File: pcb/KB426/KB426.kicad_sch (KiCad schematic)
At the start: 159 parts, among them J1 Conn_01x03_Socket, SW1 SW_Push_45deg, SW10 SW_Push_45deg, SW11 SW_Push_45deg, SW12 SW_Push_45deg, SW13 SW_Push_45deg, SW14 SW_Push_45deg, SW15 SW_Push_45deg, SW16 SW_Push_45deg, SW17 SW_Push_45deg, SW18 SW_Push_45deg, SW19 SW_Push_45deg, SW2 SW_Push_45deg, SW20 SW_Push_45deg, SW21 SW_Push_45deg, SW22 SW_Push_45deg, SW23 SW_Push_45deg, SW24 SW_Push_45deg, SW25 SW_Push_45deg, SW26 SW_Push_45deg, SW27 SW_Push_45deg, SW28 SW_Push_45deg, SW29 SW_Push_45deg, SW3 SW_Push_45deg, SW30 SW_Push_45deg, SW31 SW_Push_45deg, SW32 SW_Push_45deg, SW33 SW_Push_45deg, SW34 SW_Push_45deg, SW35 SW_Push_45deg, SW36 SW_Push_45deg, SW37 SW_Push_45deg, SW38 SW_Push_45deg, SW39 SW_Push_45deg, SW4 SW_Push_45deg, SW40 SW_Push_45deg, SW41 SW_Push_45deg, SW42 SW_Push_45deg, SW43 SW_Push_45deg, SW44 SW_Push_45deg, SW45 SW_Push_45deg, SW46 SW_Push_45deg, SW47 RotaryEncoder_Switch, SW48 SW_Push_45deg, SW49 SW_Push_45deg, SW5 SW_Push_45deg, SW50 SW_Push_45deg, SW51 SW_Push_45deg, SW52 SW_Push_45deg, SW53 SW_Push_45deg, SW54 SW_Push_45deg, SW55 SW_Push_45deg, SW56 SW_Push_45deg, SW57 SW_Push_45deg, SW58 SW_Push_45deg, SW59 SW_Push_45deg, SW6 SW_Push_45deg, SW60 SW_Push_45deg, SW61 SW_Push_45deg, SW62 SW_Push_45deg, SW63 SW_Push_45deg, SW64 SW_Push_45deg, SW65 SW_Push_45deg, SW66 SW_Push_45deg, SW67 SW_Push_45deg, SW68 SW_Push_45deg, SW7 SW_Push_45deg, SW8 SW_Push_45deg, SW9 SW_Push_45deg, U1 Pico

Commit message: update pcb
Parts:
- removed D64: 1N4148, Diode_THT:D_DO-35_SOD27_P7.62mm_Horizontal, symbol Diode:1N4148
- removed H11: MountingHole, MountingHole:MountingHole_2.2mm_M2_Pad, symbol Mechanical:MountingHole
- removed J1: Conn_01x03_Socket, Connector_PinHeader_2.54mm:PinHeader_1x03_P2.54mm_Vertical, symbol Connector:Conn_01x03_Socket
- removed ST7735S_80x160_SPI1: ~, SPI_Displays:ST7735S_80x160_SPI, symbol SPI_Displays:ST7735S_80x160_SPI
- removed SW64: SW_Push_45deg, PCM_Switch_Keyboard_Cherry_MX:SW_Cherry_MX_PCB_1.00u, symbol Switch:SW_Push_45deg
- added D47, D48: 1N4148, Diode_THT:D_DO-35_SOD27_P7.62mm_Horizontal, symbol Diode:1N4148
- added D70: LED, LED_THT:LED_D5.0mm, symbol Device:LED
- added J3: Conn_01x06_Socket, Connector_PinHeader_2.54mm:PinHeader_2x03_P2.54mm_Vertical, symbol Connector:Conn_01x06_Socket
- added R5: 390, Resistor_THT:R_Axial_DIN0207_L6.3mm_D2.5mm_P10.16mm_Horizontal, symbol Device:R
- added SSD1306_128x32_i2c1: ~, SPI_Displays:SSD1306_128x32_i2c, symbol SPI_Displays:ssd1306_128x32_i2c
- added SW47, SW69: SW_Push_45deg, PCM_Switch_Keyboard_Cherry_MX:SW_Cherry_MX_PCB_1.00u, symbol Switch:SW_Push_45deg
- C1, C2: footprint Capacitor_SMD:C_1206_3216Metric_Pad1.33x1.80mm_HandSolder -> Capacitor_THT:C_Disc_D3.0mm_W1.6mm_P2.50mm
- SW60: footprint PCM_Switch_Keyboard_Cherry_MX:SW_Cherry_MX_PCB_1.00u -> PCM_Switch_Keyboard_Cherry_MX:SW_Cherry_MX_PCB_2.25u
- SW61: footprint PCM_Switch_Keyboard_Cherry_MX:SW_Cherry_MX_PCB_2.25u -> PCM_Switch_Keyboard_Cherry_MX:SW_Cherry_MX_PCB_1.00u
- SW66: footprint PCM_Switch_Keyboard_Cherry_MX:SW_Cherry_MX_PCB_1.00u -> PCM_Switch_Keyboard_Cherry_MX:SW_Cherry_MX_PCB_1.75u
- SW68: footprint PCM_Switch_Keyboard_Cherry_MX:SW_Cherry_MX_PCB_1.75u -> PCM_Switch_Keyboard_Cherry_MX:SW_Cherry_MX_PCB_1.00u
- renumbered D48 to D64, D47 to D69, D100 to D71, R5 to R6, SW47 to SW48, SW48 to SW64
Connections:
- net +3V3: now also R5.1, SSD1306_128x32_i2c1.2 (VCC)
- net Col 1: now also SW56.2, SW63.2, J3.6 (Pin_6); no longer SW57.2, SW65.2
- net Col 2: now also SW57.2, SW64.2, J3.2 (Pin_2); no longer SW58.2, SW66.2
- net Col 3: now also SW58.2, SW65.2; no longer SW59.2, SW67.2
- net Col 4: now also SW59.2, SW66.2; no longer SW60.2, SW68.2
- net Col 5: now also SW60.2, SW67.2; no longer SW61.2
- net Col 6: now also SW61.2, SW68.2; no longer SW62.2
- net Col 7: now also SW62.2, SW47.2, SW69.2; no longer SW48.S2, SW63.2
- net Col 8: now also SW48.S1; no longer SW56.2, SW64.2
- net GND: now also D70.1 (K), J3.3 (Pin_3), J3.4 (Pin_4), SSD1306_128x32_i2c1.1 (GND)
- net Row 6: now also D47.1 (K), D48.1 (K); no longer D69.1 (K)
- net Row 7: no longer D56.1 (K)
- net Row 8: now also D56.1 (K); no longer D63.1 (K), D64.1 (K)
- net Row 9: now also D63.1 (K), D64.1 (K), D69.1 (K)
- net at U1.24 (GPIO18): now also SSD1306_128x32_i2c1.3 (SCK)
- net at U1.25 (GPIO19): now also SSD1306_128x32_i2c1.4 (SDA)
- net at U1.41 (SWCLK): now also J3.1 (Pin_1)
- net at U1.43 (SWDIO): now also J3.5 (Pin_5)
- net at D69.2 (A): now also SW69.1; no longer SW48.S1
- new net: D47.2 (A), SW47.1
- new net: D70.2 (A), R5.2
- new net: D48.2 (A), SW48.S2
- no-connect marks 1 -> 0
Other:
- moved on the sheet: C1, C2, D55, D56, D57, D58, D59, D60, D61, D62, D63, D64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

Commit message: + update pcb
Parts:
- added J2: Conn_01x03_Socket, Connector_PinHeader_2.54mm:PinHeader_1x03_P2.54mm_Vertical, symbol Connector:Conn_01x03_Socket
- renumbered C2 to C1, C1 to C2, J3 to J1, R4 to R1, R3 to R2, R2 to R3, R1 to R4
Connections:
- net +5V: now also U1.39 (VSYS), J2.1 (Pin_1)
- net Col 1: no longer J1.6 (Pin_6)
- net Col 2: no longer J1.2 (Pin_2)
- net GND: now also J2.3 (Pin_3)
- net Rot CLK: now also U1.31 (GPIO26_ADC0); no longer U1.32 (GPIO27_ADC1)
- net Rot DT: now also U1.29 (GPIO22); no longer U1.34 (GPIO28_ADC2)
- net Row 9: now also U1.24 (GPIO18); no longer U1.21 (GPIO16)
- net at U1.22 (GPIO17): now also J1.2 (Pin_2)
- net at SSD1306_128x32_i2c1.3 (SCK): now also U1.27 (GPIO21); no longer U1.24 (GPIO18)
- net at U1.25 (GPIO19): now also J2.2 (Pin_2); no longer SSD1306_128x32_i2c1.4 (SDA)
- net at U1.26 (GPIO20): now also SSD1306_128x32_i2c1.4 (SDA)
- net at R6.1: now also U1.32 (GPIO27_ADC1); no longer U1.29 (GPIO22)
- net at U1.41 (SWCLK): now also J1.5 (Pin_5); no longer J1.1 (Pin_1)
- net at U1.43 (SWDIO): now also J1.1 (Pin_1); no longer J1.5 (Pin_5)
- new net: J1.6 (Pin_6), U1.21 (GPIO16)
- no-connect marks 0 -> 4
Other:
- moved on the sheet: D71, H1, H10, H2, H3, H4, H5, H6, H7, H8, H9, J1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

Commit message: pcb v1
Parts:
- removed J2: Conn_01x03_Socket, Connector_PinHeader_2.54mm:PinHeader_1x03_P2.54mm_Vertical, symbol Connector:Conn_01x03_Socket
- added C10, C11, C12, C13, C14, C15, C16, C17, C18, C3, C4, C5, C6, C7, C8, C9: 100nF, Capacitor_SMD:C_0603_1608Metric, symbol Device:C_45deg
- added D72, D73, D74, D75, D76, D77, D78, D79, D80, D81, D82, D83, D84, D85, D86, D87: WS2812B, LED_SMD:LED_WS2812B_PLCC4_5.0x5.0mm_P3.2mm, symbol LED:WS2812B
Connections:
- net +5V: now also C10.2, C11.2, C12.2, C13.2, C14.2, C15.2, C16.2, C17.2, C18.2, C3.2, C4.2, C5.2, C6.2, C7.2, C8.2, C9.2, D72.1 (VDD), D73.1 (VDD), D74.1 (VDD), D75.1 (VDD), D76.1 (VDD), D77.1 (VDD), D78.1 (VDD), D79.1 (VDD), D80.1 (VDD), D81.1 (VDD), D82.1 (VDD), D83.1 (VDD), D84.1 (VDD), D85.1 (VDD), D86.1 (VDD), D87.1 (VDD)
- net GND: now also C10.1, C11.1, C12.1, C13.1, C14.1, C15.1, C16.1, C17.1, C18.1, C3.1, C4.1, C5.1, C6.1, C7.1, C8.1, C9.1, D72.3 (VSS), D73.3 (VSS), D74.3 (VSS), D75.3 (VSS), D76.3 (VSS), D77.3 (VSS), D78.3 (VSS), D79.3 (VSS), D80.3 (VSS), D81.3 (VSS), D82.3 (VSS), D83.3 (VSS), D84.3 (VSS), D85.3 (VSS), D86.3 (VSS), D87.3 (VSS)
- net uart rx: now reaches J1.6 (Pin_6)
- net uart rx: now also U1.22 (GPIO17); no longer U1.21 (GPIO16)
- net uart tx: now reaches J1.2 (Pin_2)
- net uart tx: now also U1.21 (GPIO16); no longer U1.22 (GPIO17)
- net leds: now reaches U1.25 (GPIO19)
- net leds: now also D72.4 (DIN)
- net swclk: now reaches J1.5 (Pin_5), U1.41 (SWCLK)
- net swdio: now reaches J1.1 (Pin_1), U1.43 (SWDIO)
- new net: D75.2 (DOUT), D76.4 (DIN)
- new net: D74.2 (DOUT), D75.4 (DIN)
- new net: D73.2 (DOUT), D74.4 (DIN)
- new net: D72.2 (DOUT), D73.4 (DIN)
- new net: D86.2 (DOUT), D87.4 (DIN)
- new net: D76.2 (DOUT), D77.4 (DIN)
- new net: D77.2 (DOUT), D78.4 (DIN)
- new net: D81.2 (DOUT), D82.4 (DIN)
- new net: D80.2 (DOUT), D81.4 (DIN)
- new net: D83.2 (DOUT), D84.4 (DIN)
- new net: D82.2 (DOUT), D83.4 (DIN)
- new net: D79.2 (DOUT), D80.4 (DIN)
- new net: D78.2 (DOUT), D79.4 (DIN)
- new net: D85.2 (DOUT), D86.4 (DIN)
- new net: D84.2 (DOUT), D85.4 (DIN)
- no-connect marks 4 -> 5
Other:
- moved on the sheet: D71, R6, SSD1306_128x32_i2c1

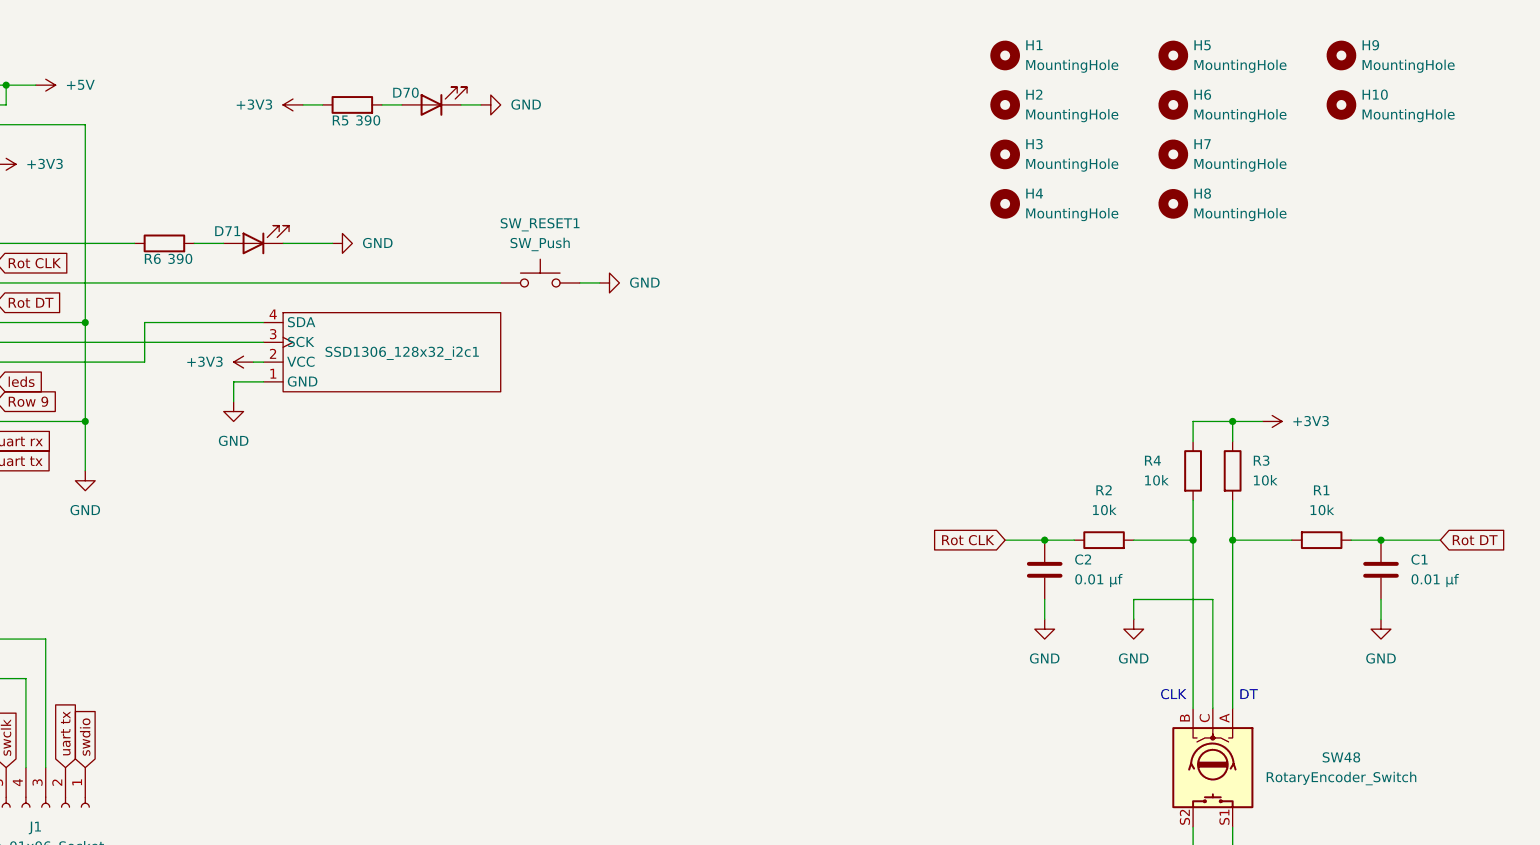
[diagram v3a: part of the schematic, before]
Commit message: fix ground plane, update serigraphie
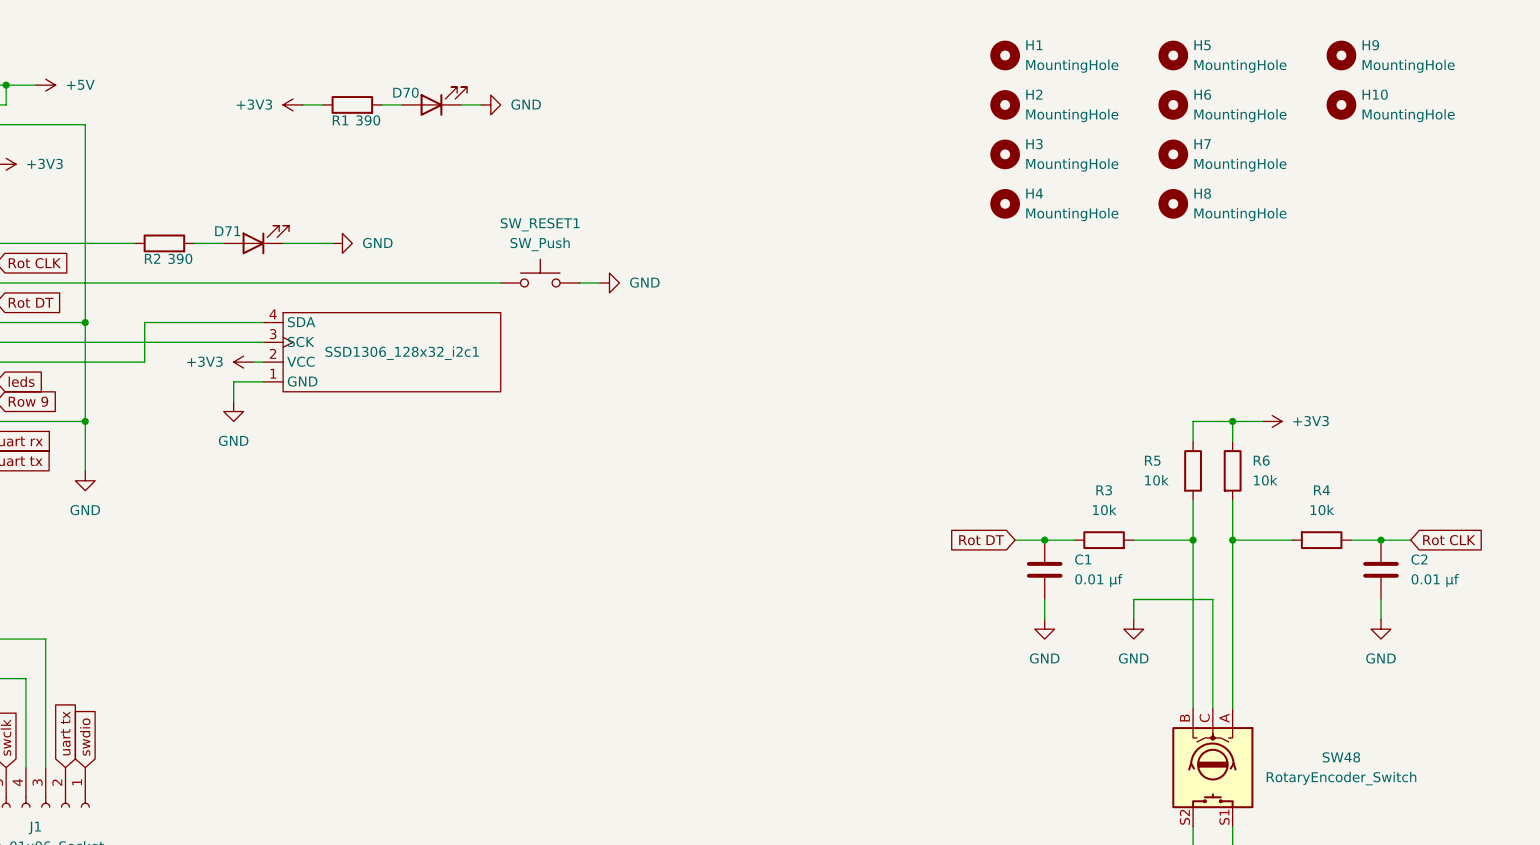
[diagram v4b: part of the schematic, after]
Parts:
- renumbered C2 to C1, C1 to C2, R5 to R1, R6 to R2, R2 to R3, R1 to R4, R4 to R5, R3 to R6
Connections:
- net Rot CLK: now also C2.1, R4.1; no longer C1.1, R3.1
- net Rot DT: now also C1.1, R3.1; no longer C2.1, R4.1
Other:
- note removed: "CLK"
- note removed: "DT"
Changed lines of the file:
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@@
 	)
 	(junction
+		(at 476.25 95.25)
+		(diameter 0)
+		(color 0 0 0 0)
+	)
+	(junction
 		(at 444.5 166.37)
 		(diameter 0)
@@
 	)
 	(junction
-		(at 519.43 95.25)
-		(diameter 0)
-		(color 0 0 0 0)
-	)
-	(junction
 		(at 317.5 219.71)
 		(diameter 0)
@@
 	)
 	(junction
+		(at 519.43 95.25)
+		(diameter 0)
+		(color 0 0 0 0)
+	)
+	(junction
 		(at 177.8 153.67)
 		(diameter 0)
@@
 	)
 	(junction
-		(at 476.25 95.25)
-		(diameter 0)
-		(color 0 0 0 0)
-	)
-	(junction
 		(at 203.2 207.01)
 		(diameter 0)
@@
 	(wire
 		(pts
-			(xy 471.17 95.25) (xy 476.25 95.25)
-		)
-		(stroke
-			(width 0)
-			(type default)
-		)
-	)
-	(wire
-		(pts
 			(xy 279.4 303.53) (xy 304.8 303.53)
 		)
@@
 	(wire
 		(pts
-			(xy 476.25 95.25) (xy 480.06 95.25)
+			(xy 472.44 95.25) (xy 476.25 95.25)
 		)
 		(stroke
@@
 	(wire
 		(pts
+			(xy 519.43 95.25) (xy 515.62 95.25)
+		)
+		(stroke
+			(width 0)
+			(type default)
+		)
+	)
+	(wire
+		(pts
 			(xy 508 248.92) (xy 203.2 248.92)
 		)
@@
 	(wire
 		(pts
+			(xy 476.25 95.25) (xy 480.06 95.25)
+		)
+		(stroke
+			(width 0)
+			(type default)
+		)
+	)
+	(wire
+		(pts
 			(xy 474.98 207.01) (xy 477.52 207.01)
 		)
@@
 	(wire
 		(pts
-			(xy 519.43 95.25) (xy 515.62 95.25)
+			(xy 523.24 95.25) (xy 519.43 95.25)
 		)
 		(stroke
@@
 	(wire
 		(pts
-			(xy 527.05 95.25) (xy 519.43 95.25)
-		)
-		(stroke
-			(width 0)
-			(type default)
-		)
-	)
-	(wire
-		(pts
 			(xy 375.92 67.31) (xy 360.68 67.31)
 		)
@@
 		)
 	)
-	(text "CLK\n"
-		(exclude_from_sim no)
-		(at 492.76 115.316 0)
-		(effects
-			(font
-				(size 1.27 1.27)
-			)
-		)
-	)
-	(text "DT"
-		(exclude_from_sim no)
-		(at 502.412 115.316 0)
-		(effects
-			(font
-				(size 1.27 1.27)
-			)
-		)
-	)
 	(global_label "swclk"
 		(shape input)
@@
 	(global_label "Rot DT"
 		(shape input)
-		(at 527.05 95.25 0)
+		(at 472.44 95.25 180)
 		(fields_autoplaced yes)
 		(effects
@@
 				(size 1.27 1.27)
 			)
-			(justify left)
+			(justify right)
 		)
 		(property "Intersheetrefs" "${INTERSHEET_REFS}"
-			(at 536.3851 95.25 0)
+			(at 463.1049 95.25 0)
 			(effects
 				(font
 					(size 1.27 1.27)
 				)
-				(justify left)
+				(justify right)
 				(hide yes)
 			)
@@
 	(global_label "Rot CLK"
 		(shape input)
-		(at 471.17 95.25 180)
+		(at 523.24 95.25 0)
 		(fields_autoplaced yes)
 		(effects
@@
 				(size 1.27 1.27)
 			)
-			(justify right)
+			(justify left)
 		)
 		(property "Intersheetrefs" "${INTERSHEET_REFS}"
-			(at 460.5044 95.25 0)
+			(at 533.9056 95.25 0)
 			(effects
 				(font
 					(size 1.27 1.27)
 				)
-				(justify right)
+				(justify left)
 				(hide yes)
 			)
@@
 		(dnp no)
 		(fields_autoplaced yes)
-		(property "Reference" "R3"
+		(property "Reference" "R6"
 			(at 502.92 85.0899 0)
 			(effects
@@
 			(project "KB426"
 				(path "/9a9ef932-5886-4734-ab54-818112b62564"
-					(reference "R3")
+					(reference "R6")
 					(unit 1)
 				)
@@
 		(on_board yes)
 		(dnp no)
-		(property "Reference" "R5"
+		(property "Reference" "R1"
 			(at 385.826 41.402 90)
 			(effects
@@
 			(project "KB426"
 				(path "/9a9ef932-5886-4734-ab54-818112b62564"
-					(reference "R5")
+					(reference "R1")
 					(unit 1)
 				)
@@
 		(dnp no)
 		(fields_autoplaced yes)
-		(property "Reference" "C1"
+		(property "Reference" "C2"
 			(at 523.24 97.7899 0)
 			(effects
@@
 			(project ""
 				(path "/9a9ef932-5886-4734-ab54-818112b62564"
-					(reference "C1")
+					(reference "C2")
 					(unit 1)
 				)
@@
 		(on_board yes)
 		(dnp no)
-		(property "Reference" "R6"
+		(property "Reference" "R2"
 			(at 361.696 59.182 90)
 			(effects
@@
 			(project "KB426"
 				(path "/9a9ef932-5886-4734-ab54-818112b62564"
-					(reference "R6")
+					(reference "R2")
 					(unit 1)
 				)
@@
 		(dnp no)
 		(fields_autoplaced yes)
-		(property "Reference" "R2"
+		(property "Reference" "R3"
 			(at 483.87 88.9 90)
 			(effects
@@
 			(project "KB426"
 				(path "/9a9ef932-5886-4734-ab54-818112b62564"
-					(reference "R2")
+					(reference "R3")
 					(unit 1)
 				)
@@
 		(dnp no)
 		(fields_autoplaced yes)
-		(property "Reference" "C2"
+		(property "Reference" "C1"
 			(at 480.06 97.7899 0)
 			(effects
@@
 			(project "KB426"
 				(path "/9a9ef932-5886-4734-ab54-818112b62564"
-					(reference "C2")
+					(reference "C1")
 					(unit 1)
 				)
@@
 		(on_board yes)
 		(dnp no)
-		(property "Reference" "R4"
+		(property "Reference" "R5"
 			(at 488.95 85.09 0)
 			(effects
@@
 			(project ""
 				(path "/9a9ef932-5886-4734-ab54-818112b62564"
-					(reference "R4")
+					(reference "R5")
 					(unit 1)
 				)
@@
 		(dnp no)
 		(fields_autoplaced yes)
-		(property "Reference" "R1"
+		(property "Reference" "R4"
 			(at 511.81 88.9 90)
 			(effects
@@
 			(project "KB426"
 				(path "/9a9ef932-5886-4734-ab54-818112b62564"
-					(reference "R1")
+					(reference "R4")
 					(unit 1)
 				)
